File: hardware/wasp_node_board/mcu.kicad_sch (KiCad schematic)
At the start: 4 parts, among them J6 TC2030, U1 STM32H723ZGTx, U3 APS6404L-3SQRx-SN, Y2 ASE-25.000MHZ-L-K-T

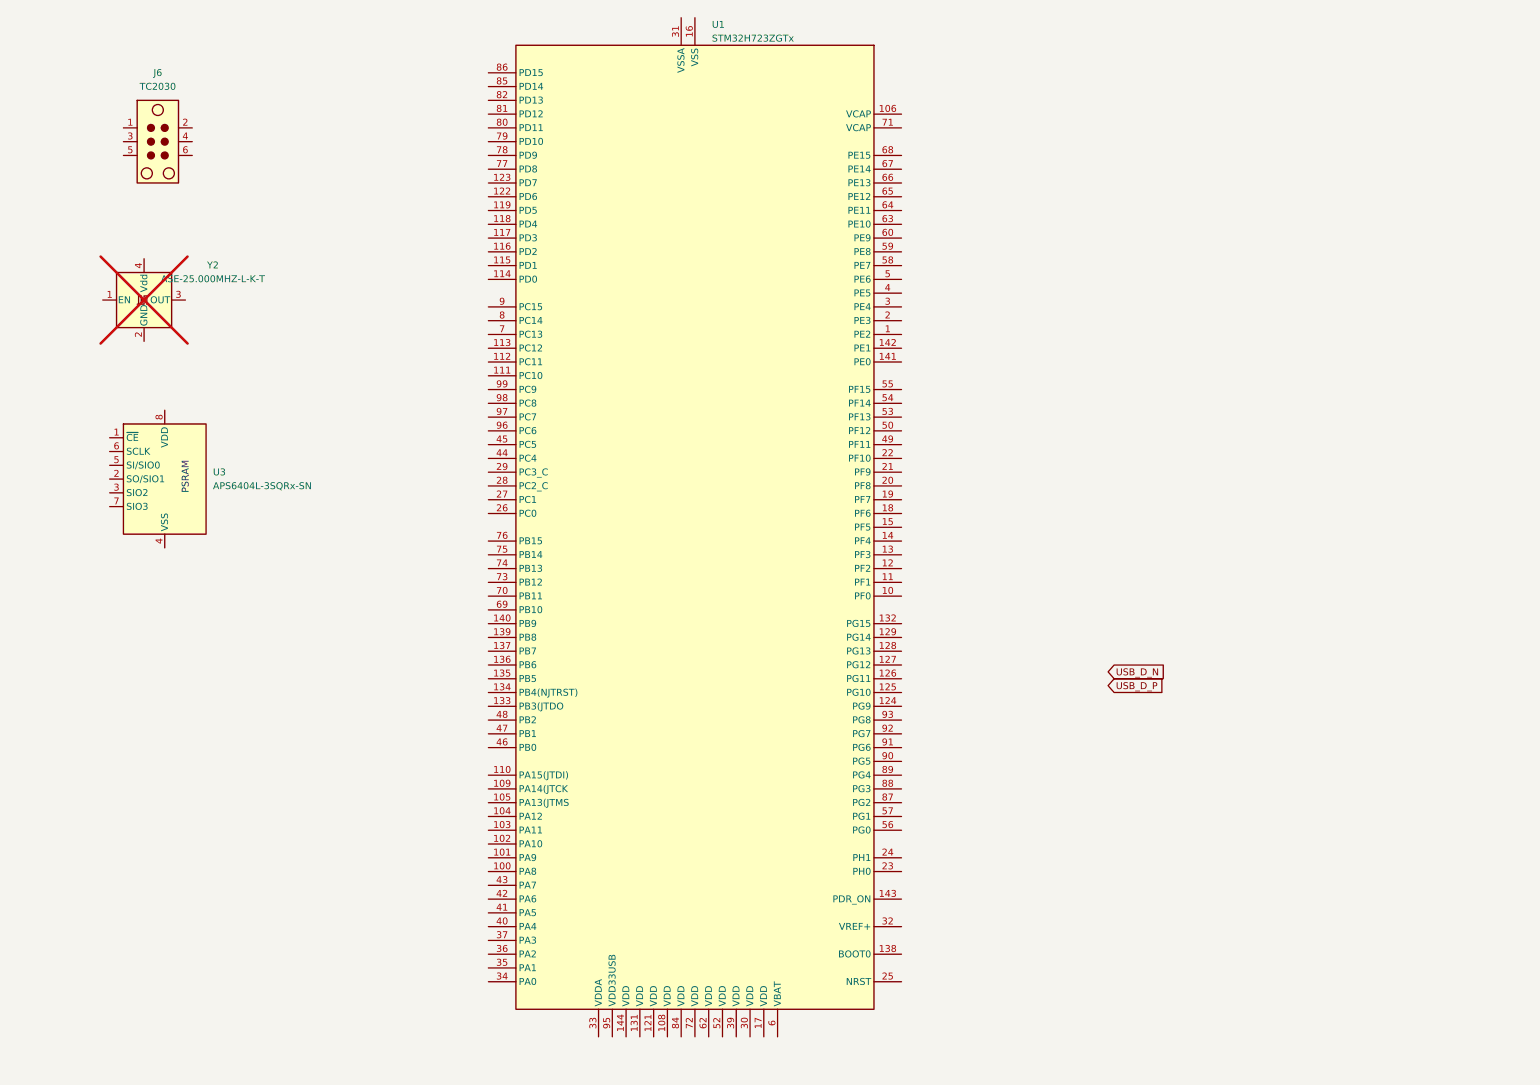
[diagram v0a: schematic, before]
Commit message: Node board schematic complete — MCU, switch, PSRAM, power and expansion
Co-Authored-By: Claude Opus 5 <noreply@anthropic.com>
Claude-Session: https://claude.ai/code/session_01R5uaLk4w44r9dBy8LCo6if
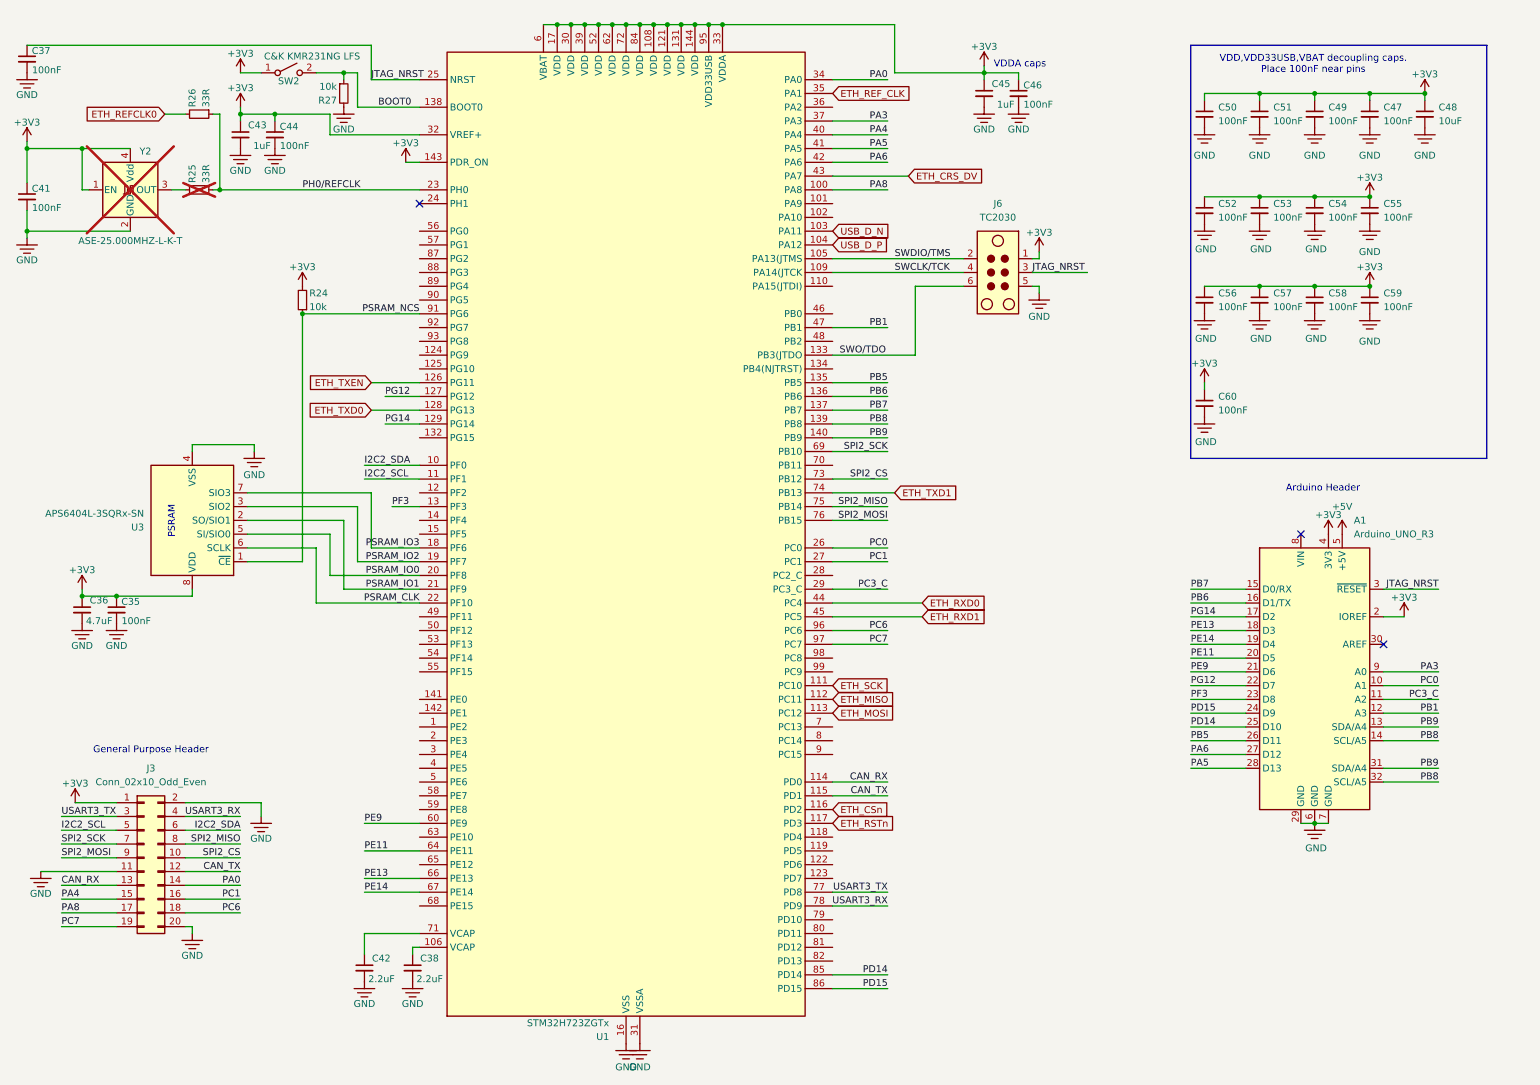
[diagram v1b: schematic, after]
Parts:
- added A1: Arduino_UNO_R3, Module:Arduino_UNO_R3_WithMountingHoles, symbol MCU_Module:Arduino_UNO_R3
- added C35, C37, C41, C44, C46, C47, C49, C50, C51, C52, C53, C54, C55, C56, C57, C58, C59, C60: 100nF, Capacitor_SMD:C_0402_1005Metric, symbol Device:C_Small
- added C36: 4.7uF, Capacitor_SMD:C_0603_1608Metric, symbol Device:C_Small
- added C38, C42: 2.2uF, Capacitor_SMD:C_0603_1608Metric, symbol Device:C_Small
- added C43, C45: 1uF, Capacitor_SMD:C_0603_1608Metric, symbol Device:C_Small
- added C48: 10uF, Capacitor_SMD:C_0805_2012Metric, symbol Device:C_Small
- added J3: Conn_02x10_Odd_Even, Connector_PinHeader_1.00mm:PinHeader_2x10_P1.00mm_Vertical, symbol Connector_Generic:Conn_02x10_Odd_Even
- added R24, R27: 10k, Resistor_SMD:R_0402_1005Metric, symbol Device:R_Small
- added R25, R26: 33R, Resistor_SMD:R_0402_1005Metric, symbol Device:R_Small
- added SW2: C&K KMR231NG LFS, Button_Switch_SMD:SW_Push_1P1T_NO_CK_KMR2, symbol Switch:SW_SPST
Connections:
- net USB_D_N: now also U1.103 (PA11)
- net USB_D_P: now also U1.104 (PA12)
- net +3V3: now reaches Y2.1 (EN)
- net +3V3: now also J6.1, U1.108 (VDD), U1.121 (VDD), U1.131 (VDD), U1.143 (PDR_ON), U1.144 (VDD), U1.17 (VDD), U1.30 (VDD), U1.32 (VREF+), U1.33 (VDDA), U1.39 (VDD), U1.52 (VDD), U1.6 (VBAT), U1.62 (VDD), U1.72 (VDD), U1.84 (VDD), U1.95 (VDD33USB), U3.8 (VDD), Y2.4 (Vdd), A1.2 (IOREF), A1.4 (3V3), C35.1, C36.1, C41.1, C43.1, C44.1, C45.1, C46.1, C47.1, C48.1, C49.1, C50.1, C51.1, C52.1, C53.1, C54.1, C55.1, C56.1, C57.1, C58.1, C59.1, C60.1, J3.1 (Pin_1), R24.2, SW2.1 (A)
- net GND: now reaches Y2.2 (GND)
- net GND: now also J6.5, U1.107 (VSS), U1.120 (VSS), U1.130 (VSS), U1.16 (VSS), U1.31 (VSSA), U1.38 (VSS), U1.51 (VSS), U1.61 (VSS), U1.83 (VSS), U1.94 (VSS), U3.4 (VSS), A1.29 (GND), A1.6 (GND), A1.7 (GND), C35.2, C36.2, C37.2, C38.2, C41.2, C42.2, C43.2, C44.2, C45.2, C46.2, C47.2, C48.2, C49.2, C50.2, C51.2, C52.2, C53.2, C54.2, C55.2, C56.2, C57.2, C58.2, C59.2, C60.2, J3.11 (Pin_11), J3.2 (Pin_2), J3.20 (Pin_20), R27.2
- net at Y2.3 (OUT): now also R25.2
- net PSRAM_NCS: now reaches U3.1 (~{CE})
- net PSRAM_NCS: now also U1.91 (PG6), R24.1
- net PSRAM_IO1: now reaches U3.2 (SO/SIO1)
- net PSRAM_IO1: now also U1.21 (PF9)
- net PSRAM_IO2: now reaches U3.3 (SIO2)
- net PSRAM_IO2: now also U1.19 (PF7)
- net PSRAM_IO0: now reaches U3.5 (SI/SIO0)
- net PSRAM_IO0: now also U1.20 (PF8)
- net PSRAM_CLK: now reaches U3.6 (SCLK)
- net PSRAM_CLK: now also U1.22 (PF10)
- net PSRAM_IO3: now reaches U3.7 (SIO3)
- net PSRAM_IO3: now also U1.18 (PF6)
- net SWDIO/TMS: now reaches J6.2
- net SWDIO/TMS: now also U1.105 (PA13(JTMS)
- net JTAG_NRST: now reaches J6.3
- net JTAG_NRST: now also U1.25 (NRST), A1.3 (~{RESET}), C37.1
- net SWCLK/TCK: now reaches J6.4
- net SWCLK/TCK: now also U1.109 (PA14(JTCK)
- net SWO/TDO: now reaches J6.6
- net SWO/TDO: now also U1.133 (PB3(JTDO)
- net I2C2_SDA: now reaches U1.10 (PF0)
- net I2C2_SDA: now also J3.6 (Pin_6)
- net PA8: now reaches U1.100 (PA8)
- net PA8: now also J3.17 (Pin_17)
- net at U1.106 (VCAP): now also C38.1
- net I2C2_SCL: now reaches U1.11 (PF1)
- net I2C2_SCL: now also J3.5 (Pin_5)
- net ETH_SCK: now reaches U1.111 (PC10)
- net ETH_MISO: now reaches U1.112 (PC11)
- net ETH_MOSI: now reaches U1.113 (PC12)
- net CAN_RX: now reaches U1.114 (PD0)
- net CAN_RX: now also J3.13 (Pin_13)
- net CAN_TX: now reaches U1.115 (PD1)
- net CAN_TX: now also J3.12 (Pin_12)
- net ETH_CSn: now reaches U1.116 (PD2)
- net ETH_RSTn: now reaches U1.117 (PD3)
- net ETH_TXEN: now reaches U1.126 (PG11)
- net PG12: now reaches U1.127 (PG12)
- net PG12: now also A1.22 (D7)
- net ETH_TXD0: now reaches U1.128 (PG13)
- net PG14: now reaches U1.129 (PG14)
- net PG14: now also A1.17 (D2)
- net PF3: now reaches U1.13 (PF3)
- net PF3: now also A1.23 (D8)
- net PB5: now reaches U1.135 (PB5)
- net PB5: now also A1.26 (D11)
- net PB6: now reaches U1.136 (PB6)
- net PB6: now also A1.16 (D1/TX)
- net PB7: now reaches U1.137 (PB7)
- net PB7: now also A1.15 (D0/RX)
- net BOOT0: now reaches U1.138 (BOOT0)
- net BOOT0: now also R27.1, SW2.2 (B)
- net PB8: now reaches U1.139 (PB8)
- net PB8: now also A1.14 (SCL/A5), A1.32 (SCL/A5)
- net PB9: now reaches U1.140 (PB9)
- net PB9: now also A1.13 (SDA/A4), A1.31 (SDA/A4)
- net PH0/REFCLK: now reaches U1.23 (PH0)
- net PH0/REFCLK: now also R25.1, R26.1
- net PC0: now reaches U1.26 (PC0)
- net PC0: now also A1.10 (A1)
- net PC1: now reaches U1.27 (PC1)
- net PC1: now also J3.16 (Pin_16)
- net PC3_C: now reaches U1.29 (PC3_C)
- net PC3_C: now also A1.11 (A2)
- net PA0: now reaches U1.34 (PA0)
- net PA0: now also J3.14 (Pin_14)
- net ETH_REF_CLK: now reaches U1.35 (PA1)
- net PA3: now reaches U1.37 (PA3)
- net PA3: now also A1.9 (A0)
- net PA4: now reaches U1.40 (PA4)
- net PA4: now also J3.15 (Pin_15)
- net PA5: now reaches U1.41 (PA5)
- net PA5: now also A1.28 (D13)
- net PA6: now reaches U1.42 (PA6)
- net PA6: now also A1.27 (D12)
- net ETH_CRS_DV: now reaches U1.43 (PA7)
- net ETH_RXD0: now reaches U1.44 (PC4)
- net ETH_RXD1: now reaches U1.45 (PC5)
- net PB1: now reaches U1.47 (PB1)
- net PB1: now also A1.12 (A3)
- net PE9: now reaches U1.60 (PE9)
- net PE9: now also A1.21 (D6)
- net PE11: now reaches U1.64 (PE11)
- net PE11: now also A1.20 (D5)
- net PE13: now reaches U1.66 (PE13)
- net PE13: now also A1.18 (D3)
- net PE14: now reaches U1.67 (PE14)
- net PE14: now also A1.19 (D4)
- net SPI2_SCK: now reaches U1.69 (PB10)
- net SPI2_SCK: now also J3.7 (Pin_7)
- net at U1.71 (VCAP): now also C42.1
- net SPI2_CS: now reaches U1.73 (PB12)
- net SPI2_CS: now also J3.10 (Pin_10)
- net ETH_TXD1: now reaches U1.74 (PB13)
- net SPI2_MISO: now reaches U1.75 (PB14)
- net SPI2_MISO: now also J3.8 (Pin_8)
- net SPI2_MOSI: now reaches U1.76 (PB15)
- net SPI2_MOSI: now also J3.9 (Pin_9)
- net USART3_TX: now reaches U1.77 (PD8)
- net USART3_TX: now also J3.3 (Pin_3)
- net USART3_RX: now reaches U1.78 (PD9)
- net USART3_RX: now also J3.4 (Pin_4)
- net PD14: now reaches U1.85 (PD14)
- net PD14: now also A1.25 (D10)
- net PD15: now reaches U1.86 (PD15)
- net PD15: now also A1.24 (D9)
- net PC6: now reaches U1.96 (PC6)
- net PC6: now also J3.18 (Pin_18)
- net PC7: now reaches U1.97 (PC7)
- net PC7: now also J3.19 (Pin_19)
- new net +5V: A1.5 (+5V)
- new net ETH_REFCLK0: R26.2
- no-connect marks 0 -> 3
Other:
- note added: "Arduino Header"
- note added: "General Purpose Header"
- note added: "VDD,VDD33USB,VBAT decoupling caps. Place 100nF near pins"
- note added: "VDDA caps"
- moved on the sheet: J6, U1, U3, Y2

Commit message: Schematic verified clean and layout started
Co-Authored-By: Claude Opus 5 <noreply@anthropic.com>
Claude-Session: https://claude.ai/code/session_01R5uaLk4w44r9dBy8LCo6if
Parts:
- A1: footprint Module:Arduino_UNO_R3_WithMountingHoles -> Arduino_UNO_R3_Headers:Arduino_UNO_R3_Headers
- J3: footprint Connector_PinHeader_1.00mm:PinHeader_2x10_P1.00mm_Vertical -> Connector_PinHeader_2.54mm:PinHeader_2x10_P2.54mm_Vertical
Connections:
- no-connect marks 3 -> 56
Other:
- moved on the sheet: A1, C47, C48, C49, C50, C51, C52, C53, C54, C55, C56, C57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
